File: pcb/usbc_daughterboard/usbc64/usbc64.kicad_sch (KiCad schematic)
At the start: 12 parts, among them J1 USB_C_Receptacle_USB2.0, J2 Conn_01x04, J3 Conn_01x04, U1 ESDALD05UG4

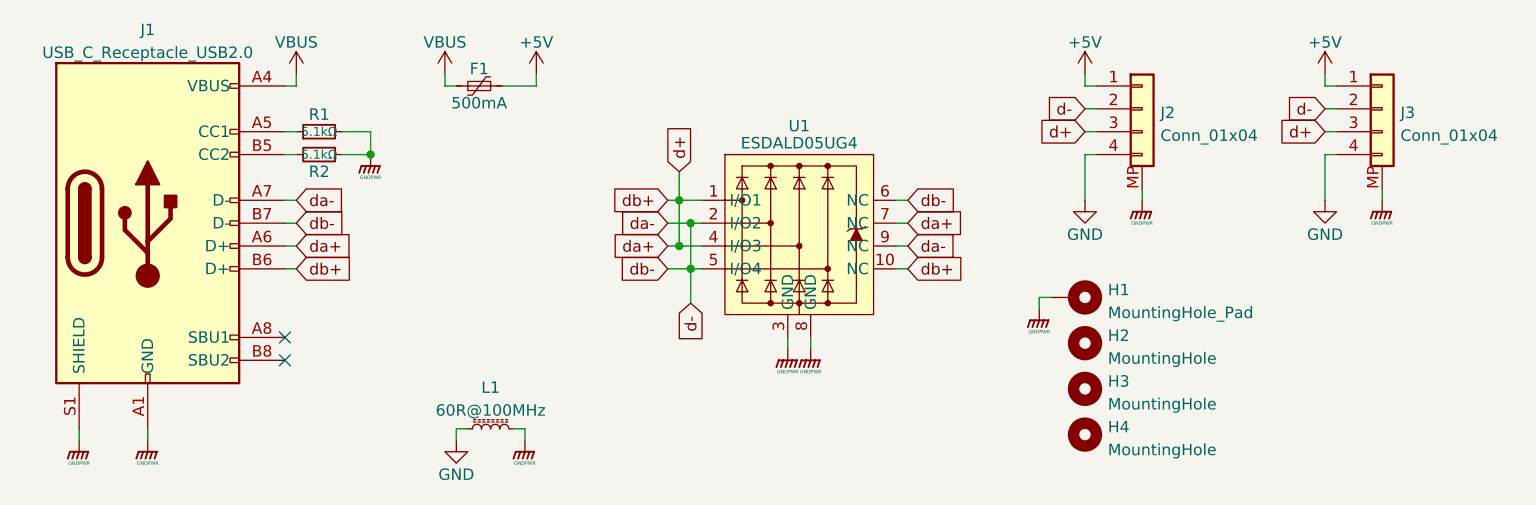
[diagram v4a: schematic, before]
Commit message: JST-SH & logo & traces routed
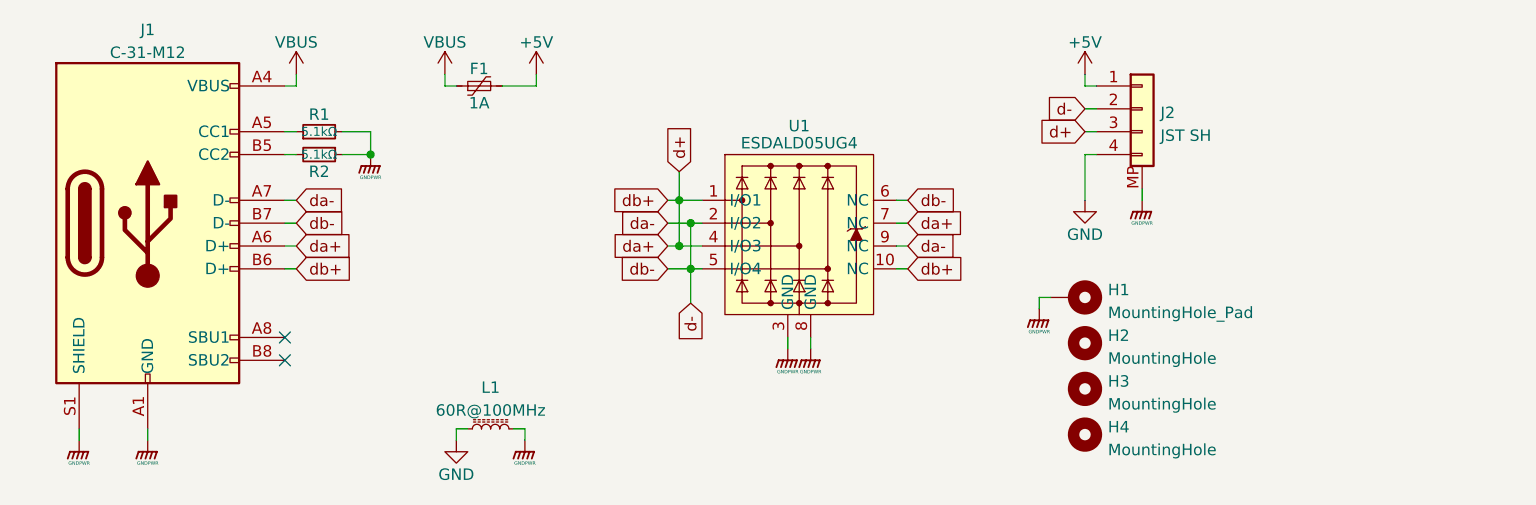
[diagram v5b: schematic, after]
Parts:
- removed J3: Conn_01x04, Connector_JST:JST_SH_SM04B-SRSS-TB_1x04-1MP_P1.00mm_Horizontal, symbol Connector_Generic:Conn_01x04
- F1: value 500mA -> 1A
- J1: value USB_C_Receptacle_USB2.0 -> C-31-M12
- J2: value Conn_01x04 -> JST SH; footprint Connector_JST:JST_SUR_SM04B-SURS-TF_1x04-1MP_P0.80mm_Horizontal -> Connector_JST:JST_SH_SM04B-SRSS-TB_1x04-1MP_P1.00mm_Horizontal
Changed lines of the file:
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@@
-    (stroke (width 0) (type default) (color 0 0 0 0))
-  )
-  (wire (pts (xy 179.705 47.625) (xy 180.975 47.625))
     (stroke (width 0) (type default) (color 0 0 0 0))
   )
@@
     (stroke (width 0) (type default) (color 0 0 0 0))
   )
-  (wire (pts (xy 179.705 41.275) (xy 179.705 42.545))
-    (stroke (width 0) (type default) (color 0 0 0 0))
-  )
   (wire (pts (xy 153.035 41.275) (xy 153.035 42.545))
     (stroke (width 0) (type default) (color 0 0 0 0))
@@
     (stroke (width 0) (type default) (color 0 0 0 0))
   )
-  (wire (pts (xy 180.975 50.165) (xy 179.705 50.165))
-    (stroke (width 0) (type default) (color 0 0 0 0))
-  )
   (wire (pts (xy 107.95 55.245) (xy 110.49 55.245))
     (stroke (width 0) (type default) (color 0 0 0 0))
@@
     (stroke (width 0) (type default) (color 0 0 0 0))
   )
-  (wire (pts (xy 179.705 45.085) (xy 180.975 45.085))
-    (stroke (width 0) (type default) (color 0 0 0 0))
-  )
   (wire (pts (xy 106.68 62.865) (xy 109.22 62.865))
     (stroke (width 0) (type default) (color 0 0 0 0))
@@
   )
   (wire (pts (xy 64.135 47.625) (xy 65.405 47.625))
-    (stroke (width 0) (type default) (color 0 0 0 0))
-  )
-  (wire (pts (xy 179.705 42.545) (xy 180.975 42.545))
-    (stroke (width 0) (type default) (color 0 0 0 0))
-  )
-  (wire (pts (xy 186.055 53.975) (xy 186.055 55.245))
-    (stroke (width 0) (type default) (color 0 0 0 0))
-  )
-  (wire (pts (xy 179.705 50.165) (xy 179.705 55.245))
     (stroke (width 0) (type default) (color 0 0 0 0))
   )
@@
     )
   )
-  (global_label "d-" (shape input) (at 179.705 45.085 180) (fields_autoplaced)
-    (effects (font (size 1.27 1.27)) (justify right))
-    (property "Intersheet References" "${INTERSHEET_REFS}" (id 0) (at 174.5705 45.1644 0)
-      (effects (font (size 1.27 1.27)) (justify right) hide)
-    )
-  )
   (global_label "da+" (shape input) (at 133.35 57.785 0) (fields_autoplaced)
     (effects (font (size 1.27 1.27)) (justify left))
@@
     )
   )
-  (global_label "d+" (shape input) (at 179.705 47.625 180) (fields_autoplaced)
-    (effects (font (size 1.27 1.27)) (justify right))
-    (property "Intersheet References" "${INTERSHEET_REFS}" (id 0) (at 174.5705 47.7044 0)
-      (effects (font (size 1.27 1.27)) (justify right) hide)
-    )
-  )
   (global_label "db-" (shape input) (at 133.35 55.245 0) (fields_autoplaced)
     (effects (font (size 1.27 1.27)) (justify left))
@@
     (in_bom yes) (on_board yes)
     (property "Reference" "F1" (id 0) (at 85.725 40.64 90))
-    (property "Value" "500mA" (id 1) (at 85.725 44.45 90))
+    (property "Value" "1A" (id 1) (at 85.725 44.45 90))
     (property "Footprint" "Fuse:Fuse_1206_3216Metric" (id 2) (at 90.805 41.275 0)
       (effects (font (size 1.27 1.27)) (justify left) hide)
@@
     (pin "1")
   )
-  (symbol (lib_id "power:+5V") (at 179.705 41.275 0) (unit 1)
-    (in_bom yes) (on_board yes) (fields_autoplaced)
-    (property "Reference" "#PWR0115" (id 0) (at 179.705 45.085 0)
-      (effects (font (size 1.27 1.27)) hide)
-    )
-    (property "Value" "+5V" (id 1) (at 179.705 37.6992 0))
-    (property "Footprint" "" (id 2) (at 179.705 41.275 0)
-      (effects (font (size 1.27 1.27)) hide)
-    )
-    (property "Datasheet" "" (id 3) (at 179.705 41.275 0)
-      (effects (font (size 1.27 1.27)) hide)
-    )
-    (pin "1")
-  )
   (symbol (lib_id "Mechanical:MountingHole") (at 153.035 81.28 0) (unit 1)
     (in_bom yes) (on_board yes) (fields_autoplaced)
@@
     )
     (pin "1")
-  )
-  (symbol (lib_id "Connector_Generic:Conn_01x04") (at 186.055 45.085 0) (unit 1)
-    (in_bom yes) (on_board yes) (fields_autoplaced)
-    (property "Reference" "J3" (id 0) (at 188.087 45.5203 0)
-      (effects (font (size 1.27 1.27)) (justify left))
-    )
-    (property "Value" "Conn_01x04" (id 1) (at 188.087 48.0572 0)
-      (effects (font (size 1.27 1.27)) (justify left))
-    )
-    (property "Footprint" "Connector_JST:JST_SH_SM04B-SRSS-TB_1x04-1MP_P1.00mm_Horizontal" (id 2) (at 186.055 45.085 0)
-      (effects (font (size 1.27 1.27)) hide)
-    )
-    (property "Datasheet" "~" (id 3) (at 186.055 45.085 0)
-      (effects (font (size 1.27 1.27)) hide)
-    )
-    (pin "1")
-    (pin "2")
-    (pin "3")
-    (pin "4")
-    (pin "MP")
   )
   (symbol (lib_id "Mechanical:MountingHole_Pad") (at 151.765 66.04 270) (unit 1)
@@
     )
     (property "Datasheet" "" (id 3) (at 73.66 51.435 0)
-      (effects (font (size 1.27 1.27)) hide)
-    )
-    (pin "1")
-  )
-  (symbol (lib_id "power:GND") (at 179.705 55.245 0) (unit 1)
-    (in_bom yes) (on_board yes)
-    (property "Reference" "#PWR0103" (id 0) (at 179.705 61.595 0)
-      (effects (font (size 1.27 1.27)) hide)
-    )
-    (property "Value" "GND" (id 1) (at 179.705 59.055 0))
-    (property "Footprint" "" (id 2) (at 179.705 55.245 0)
-      (effects (font (size 1.27 1.27)) hide)
-    )
-    (property "Datasheet" "" (id 3) (at 179.705 55.245 0)
       (effects (font (size 1.27 1.27)) hide)
     )
@@
   (symbol (lib_id "power:GNDPWR") (at 159.385 55.245 0) (unit 1)
     (in_bom yes) (on_board yes)
-    (property "Reference" "#PWR?" (id 0) (at 159.385 60.325 0)
+    (property "Reference" "#PWR0117" (id 0) (at 159.385 60.325 0)
       (effects (font (size 1.27 1.27)) hide)
     )
@@
       (effects (font (size 1.27 1.27)) (justify left))
     )
-    (property "Value" "Conn_01x04" (id 1) (at 161.417 48.0572 0)
-      (effects (font (size 1.27 1.27)) (justify left))
-    )
-    (property "Footprint" "Connector_JST:JST_SUR_SM04B-SURS-TF_1x04-1MP_P0.80mm_Horizontal" (id 2) (at 159.385 45.085 0)
+    (property "Value" "JST SH" (id 1) (at 161.417 48.0572 0)
+      (effects (font (size 1.27 1.27)) (justify left))
+    )
+    (property "Footprint" "Connector_JST:JST_SH_SM04B-SRSS-TB_1x04-1MP_P1.00mm_Horizontal" (id 2) (at 159.385 45.085 0)
       (effects (font (size 1.27 1.27)) hide)
     )
@@
     (pin "1")
   )
-  (symbol (lib_id "power:GNDPWR") (at 186.055 55.245 0) (unit 1)
-    (in_bom yes) (on_board yes)
-    (property "Reference" "#PWR?" (id 0) (at 186.055 60.325 0)
-      (effects (font (size 1.27 1.27)) hide)
-    )
-    (property "Value" "GNDPWR" (id 1) (at 186.055 57.785 0)
-      (effects (font (size 0.381 0.381)))
-    )
-    (property "Footprint" "" (id 2) (at 186.055 56.515 0)
-      (effects (font (size 1.27 1.27)) hide)
-    )
-    (property "Datasheet" "" (id 3) (at 186.055 56.515 0)
-      (effects (font (size 1.27 1.27)) hide)
-    )
-    (pin "1")
-  )
   (symbol (lib_id "Connector:USB_C_Receptacle_USB2.0") (at 48.895 57.785 0) (unit 1)
     (in_bom yes) (on_board yes) (fields_autoplaced)
     (property "Reference" "J1" (id 0) (at 48.895 36.3052 0))
-    (property "Value" "USB_C_Receptacle_USB2.0" (id 1) (at 48.895 38.8421 0))
+    (property "Value" "C-31-M12" (id 1) (at 48.895 38.8421 0))
     (property "Footprint" "Connector_USB:USB_C_Receptacle_HRO_TYPE-C-31-M-12" (id 2) (at 52.705 57.785 0)
       (effects (font (size 1.27 1.27)) hide)
@@
       (reference "#PWR0102") (unit 1) (value "GND") (footprint "")
     )
-    (path "/48b2f0d9-af73-492f-bc34-bb84d4f5653c"
-      (reference "#PWR0103") (unit 1) (value "GND") (footprint "")
-    )
     (path "/dd395997-e60e-49d7-89eb-a27b2fa000eb"
       (reference "#PWR0104") (unit 1) (value "+5V") (footprint "")
@@
       (reference "#PWR0114") (unit 1) (value "GNDPWR") (footprint "")
     )
-    (path "/16fcd392-d1f5-436f-ac8a-30839f49d2b7"
-      (reference "#PWR0115") (unit 1) (value "+5V") (footprint "")
-    )
     (path "/c1316690-7f6b-4786-9e0f-6a8acf97b1df"
-      (reference "#PWR?") (unit 1) (value "GNDPWR") (footprint "")
-    )
-    (path "/e7880dc5-89aa-4b41-be2d-83e1d26de574"
-      (reference "#PWR?") (unit 1) (value "GNDPWR") (footprint "")
+      (reference "#PWR0117") (unit 1) (value "GNDPWR") (footprint "")
     )
     (path "/062791e6-12f0-44fc-90f6-45f64ecdec87"
-      (reference "F1") (unit 1) (value "500mA") (footprint "Fuse:Fuse_1206_3216Metric")
+      (reference "F1") (unit 1) (value "1A") (footprint "Fuse:Fuse_1206_3216Metric")
     )
     (path "/22294464-5c73-43d3-ae56-8a26bed6f964"
@@
     )
     (path "/f597188e-ece8-4dde-a990-5b3388b8413b"
-      (reference "J1") (unit 1) (value "USB_C_Receptacle_USB2.0") (footprint "Connector_USB:USB_C_Receptacle_HRO_TYPE-C-31-M-12")
+      (reference "J1") (unit 1) (value "C-31-M12") (footprint "Connector_USB:USB_C_Receptacle_HRO_TYPE-C-31-M-12")
     )
     (path "/cd726dfb-75c1-4059-917b-4b8bdbb165f7"
-      (reference "J2") (unit 1) (value "Conn_01x04") (footprint "Connector_JST:JST_SUR_SM04B-SURS-TF_1x04-1MP_P0.80mm_Horizontal")
-    )
-    (path "/1de4ded6-4f8b-4fe8-94b5-bce125dc0a0c"
-      (reference "J3") (unit 1) (value "Conn_01x04") (footprint "Connector_JST:JST_SH_SM04B-SRSS-TB_1x04-1MP_P1.00mm_Horizontal")
+      (reference "J2") (unit 1) (value "JST SH") (footprint "Connector_JST:JST_SH_SM04B-SRSS-TB_1x04-1MP_P1.00mm_Horizontal")
     )
     (path "/2c0615eb-8c90-4863-b69f-db2bf5c67233"

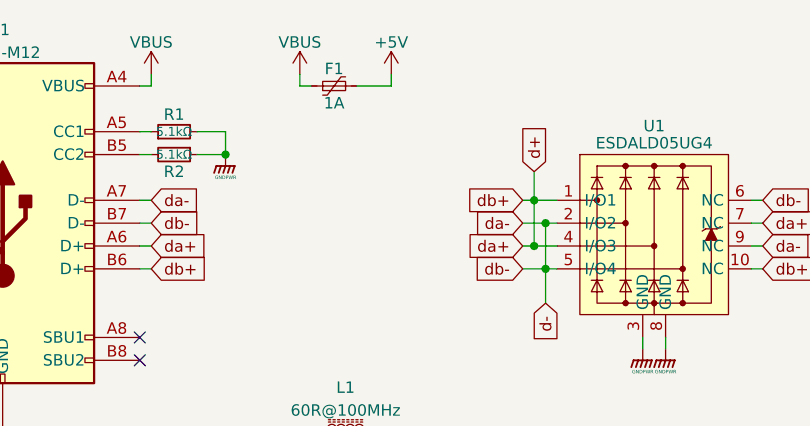
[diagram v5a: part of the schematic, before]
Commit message: diff layout + tvs diode
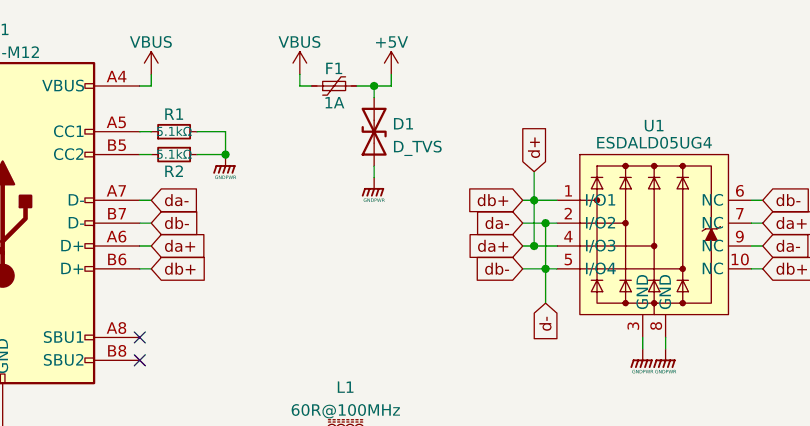
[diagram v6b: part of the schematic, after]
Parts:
- added D1: D_TVS, Diode_SMD:D_SOD-123F, symbol Device:D_TVS
- R1, R2: footprint Resistor_SMD:R_0805_2012Metric -> Resistor_SMD:R_0603_1608Metric
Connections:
- net +5V: now also D1.2 (A2)
- net GNDPWR: now also D1.1 (A1)
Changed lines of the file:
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@@
   (junction (at 73.66 50.165) (diameter 0) (color 0 0 0 0)
+  )
+  (junction (at 90.17 42.545) (diameter 0) (color 0 0 0 0)
   )
   (junction (at 109.22 62.865) (diameter 0) (color 0 0 0 0)
@@
     (stroke (width 0) (type default) (color 0 0 0 0))
   )
+  (wire (pts (xy 90.17 42.545) (xy 90.17 43.815))
+    (stroke (width 0) (type default) (color 0 0 0 0))
+  )
   (wire (pts (xy 65.405 55.245) (xy 64.135 55.245))
     (stroke (width 0) (type default) (color 0 0 0 0))
@@
     (stroke (width 0) (type default) (color 0 0 0 0))
   )
+  (wire (pts (xy 90.17 42.545) (xy 92.075 42.545))
+    (stroke (width 0) (type default) (color 0 0 0 0))
+  )
   (wire (pts (xy 83.185 80.645) (xy 84.455 80.645))
     (stroke (width 0) (type default) (color 0 0 0 0))
@@
     (stroke (width 0) (type default) (color 0 0 0 0))
   )
-  (wire (pts (xy 88.265 42.545) (xy 92.075 42.545))
+  (wire (pts (xy 88.265 42.545) (xy 90.17 42.545))
     (stroke (width 0) (type default) (color 0 0 0 0))
   )
@@
   )
   (wire (pts (xy 64.135 47.625) (xy 65.405 47.625))
+    (stroke (width 0) (type default) (color 0 0 0 0))
+  )
+  (wire (pts (xy 90.17 51.435) (xy 90.17 52.705))
     (stroke (width 0) (type default) (color 0 0 0 0))
   )
@@
     (pin "1")
   )
+  (symbol (lib_id "power:GNDPWR") (at 90.17 52.705 0) (unit 1)
+    (in_bom yes) (on_board yes)
+    (property "Reference" "#PWR0103" (id 0) (at 90.17 57.785 0)
+      (effects (font (size 1.27 1.27)) hide)
+    )
+    (property "Value" "GNDPWR" (id 1) (at 90.17 55.245 0)
+      (effects (font (size 0.381 0.381)))
+    )
+    (property "Footprint" "" (id 2) (at 90.17 53.975 0)
+      (effects (font (size 1.27 1.27)) hide)
+    )
+    (property "Datasheet" "" (id 3) (at 90.17 53.975 0)
+      (effects (font (size 1.27 1.27)) hide)
+    )
+    (pin "1")
+  )
   (symbol (lib_id "power:GNDPWR") (at 90.805 81.915 0) (unit 1)
     (in_bom yes) (on_board yes)
@@
     (pin "2")
   )
+  (symbol (lib_id "Device:D_TVS") (at 90.17 47.625 90) (unit 1)
+    (in_bom yes) (on_board yes) (fields_autoplaced)
+    (property "Reference" "D1" (id 0) (at 92.202 46.7903 90)
+      (effects (font (size 1.27 1.27)) (justify right))
+    )
+    (property "Value" "D_TVS" (id 1) (at 92.202 49.3272 90)
+      (effects (font (size 1.27 1.27)) (justify right))
+    )
+    (property "Footprint" "Diode_SMD:D_SOD-123F" (id 2) (at 90.17 47.625 0)
+      (effects (font (size 1.27 1.27)) hide)
+    )
+    (property "Datasheet" "~" (id 3) (at 90.17 47.625 0)
+      (effects (font (size 1.27 1.27)) hide)
+    )
+    (pin "1")
+    (pin "2")
+  )
   (symbol (lib_id "power:GNDPWR") (at 73.66 50.165 0) (unit 1)
     (in_bom yes) (on_board yes)
@@
       (effects (font (size 1 1)))
     )
-    (property "Footprint" "Resistor_SMD:R_0805_2012Metric" (id 2) (at 67.945 47.625 0)
+    (property "Footprint" "Resistor_SMD:R_0603_1608Metric" (id 2) (at 67.945 47.625 0)
       (effects (font (size 1.27 1.27)) hide)
     )
@@
       (effects (font (size 1 1)))
     )
-    (property "Footprint" "Resistor_SMD:R_0805_2012Metric" (id 2) (at 67.945 50.165 0)
+    (property "Footprint" "Resistor_SMD:R_0603_1608Metric" (id 2) (at 67.945 50.165 0)
       (effects (font (size 1.27 1.27)) hide)
     )
@@
       (reference "#PWR0102") (unit 1) (value "GND") (footprint "")
     )
+    (path "/0c54f784-a86d-4b78-8f66-3d2188117bec"
+      (reference "#PWR0103") (unit 1) (value "GNDPWR") (footprint "")
+    )
     (path "/dd395997-e60e-49d7-89eb-a27b2fa000eb"
       (reference "#PWR0104") (unit 1) (value "+5V") (footprint "")
@@
       (reference "#PWR0117") (unit 1) (value "GNDPWR") (footprint "")
     )
+    (path "/3845cbee-ea08-46cd-82cd-c172d1323e6f"
+      (reference "D1") (unit 1) (value "D_TVS") (footprint "Diode_SMD:D_SOD-123F")
+    )
     (path "/062791e6-12f0-44fc-90f6-45f64ecdec87"
       (reference "F1") (unit 1) (value "1A") (footprint "Fuse:Fuse_1206_3216Metric")
@@
     )
     (path "/6a21673a-3f51-446a-b166-781692c02cd4"
-      (reference "R1") (unit 1) (value "5.1kΩ") (footprint "Resistor_SMD:R_0805_2012Metric")
+      (reference "R1") (unit 1) (value "5.1kΩ") (footprint "Resistor_SMD:R_0603_1608Metric")
     )
     (path "/b65bd4ea-0413-46b5-9e69-2c80dbc4b53c"
-      (reference "R2") (unit 1) (value "5.1kΩ") (footprint "Resistor_SMD:R_0805_2012Metric")
+      (reference "R2") (unit 1) (value "5.1kΩ") (footprint "Resistor_SMD:R_0603_1608Metric")
     )
     (path "/a6f9bf39-ab6c-4e85-8e29-1b6c85263359"

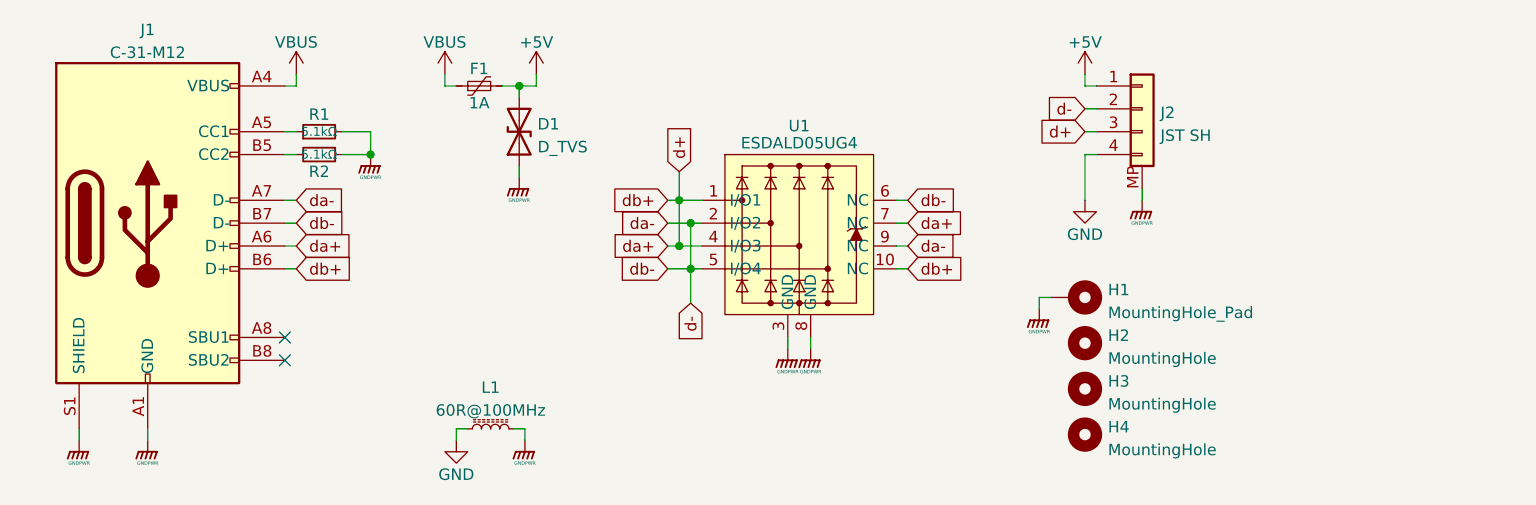
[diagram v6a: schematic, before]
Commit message: ref des silks, status LED, LED resistor, 0603 footprints, all routed
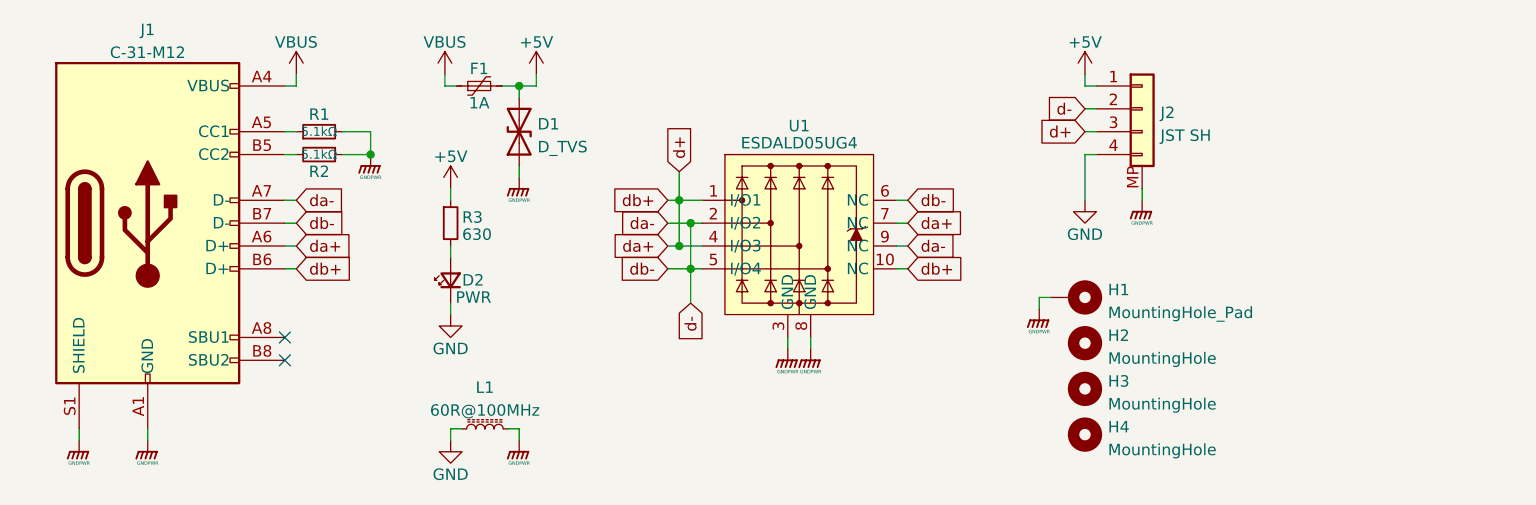
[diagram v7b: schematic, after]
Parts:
- added D2: PWR, LED_SMD:LED_0603_1608Metric, symbol Device:LED_Small
- added R3: 630, Resistor_SMD:R_0603_1608Metric, symbol Device:R_Small
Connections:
- net +5V: now also R3.1
- net GND: now also D2.1 (K)
- new net: D2.2 (A), R3.2
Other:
- moved on the sheet: L1
